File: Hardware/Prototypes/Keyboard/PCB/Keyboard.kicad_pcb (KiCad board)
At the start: 2 copper layers, 30.5 x 18.5 mm, 21 parts, among them CON1 USB-MICRO-B, U1 ATMEGA32U4-QFN44, X1 CRYSTAL-4pin

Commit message: Added the first version of the keyboard prototype module
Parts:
- removed C3: 10n, SMD-DiscreteB:0402-1005
- removed CON1: USB-MICRO-B, SMD-Connectors:USB-MICRO
- added USB1: TO HOST, Edge-Connectors:USB_EDGE, B.Cu at (149.0, 104.8)
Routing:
- net GNDD: track 14.8 -> 0.00 mm
- net Net-(R2-Pad2): track 2.57 -> 13.5 mm, vias 0 -> 1
- net Net-(R1-Pad1): track 2.71 -> 13.7 mm, vias 0 -> 1
- net +5VD: track 4.87 -> 13.0 mm, vias 0 -> 1
- net GND: track 110.6 -> 117.9 mm
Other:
- board size 30.5 x 18.5 mm -> 44.2 x 18.5 mm
- rule solder_mask_min_width: 0.1524 -> 0.0762

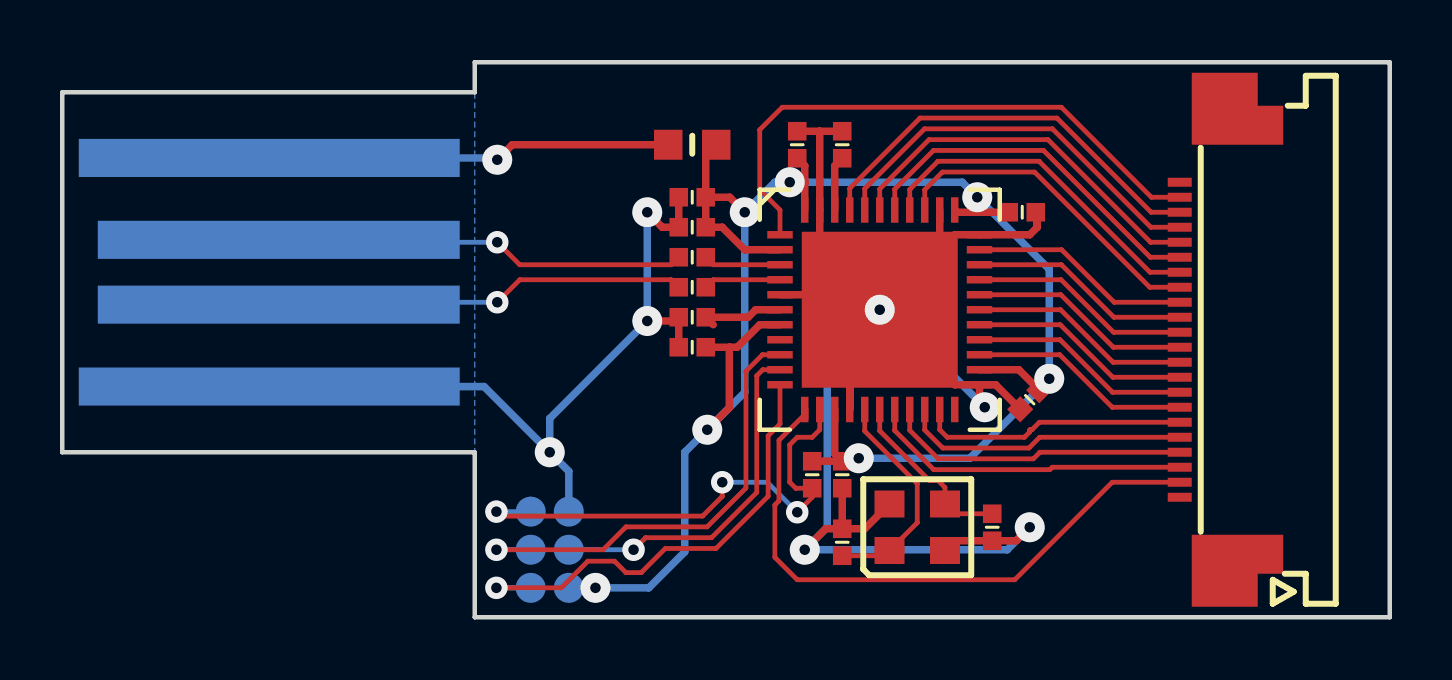
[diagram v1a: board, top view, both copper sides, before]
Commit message: More work on the keyboard
Also an attempt to make an I2C based keyboard
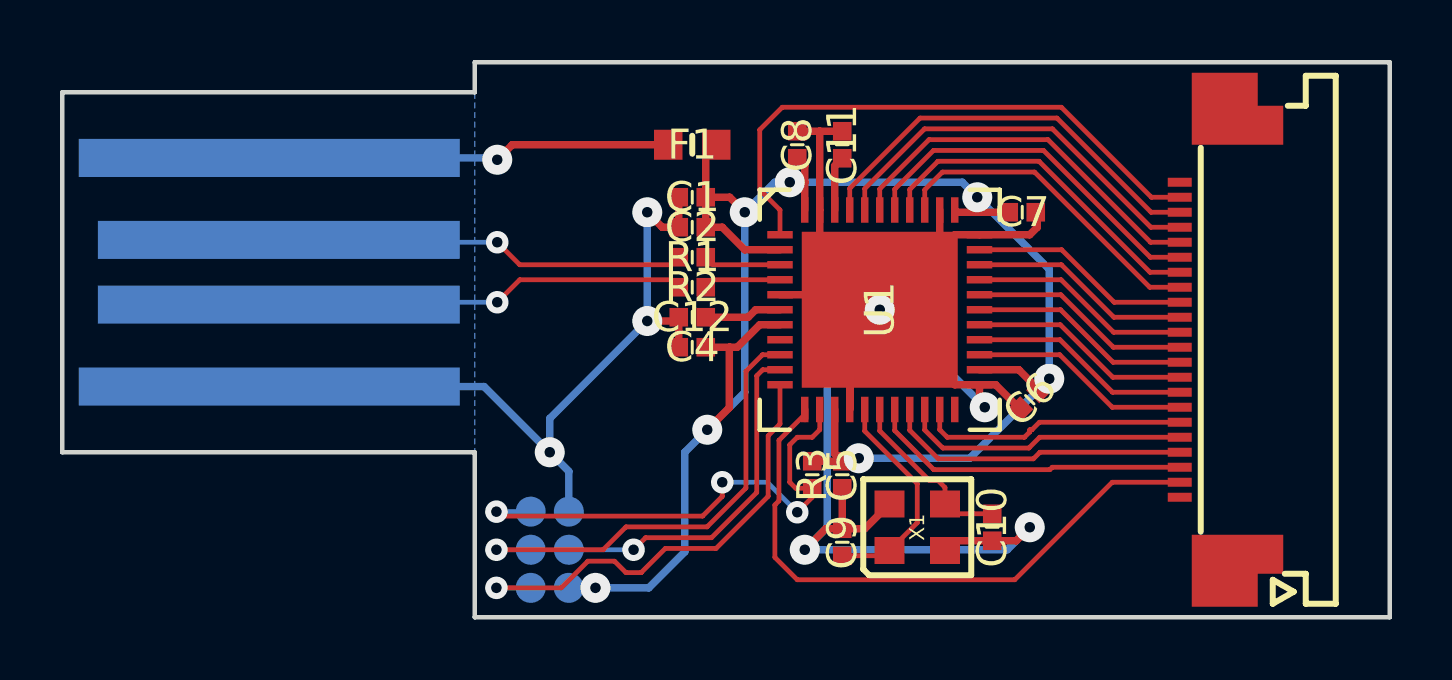
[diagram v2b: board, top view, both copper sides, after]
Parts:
- C1, C11, C12, C2, C4, C5, C6, C7, C8: footprint SMD-DiscreteB:0402-1005 -> SMD-DiscreteB:C-0402-1005
- C10, C9: value 22p -> 10p; footprint SMD-DiscreteB:0402-1005 -> SMD-DiscreteB:C-0402-1005
- R1, R2, R3: footprint SMD-DiscreteB:0402-1005 -> SMD-DiscreteB:R-0402-1005
- X1: value CRYSTAL-4pin -> ABM10-16.000MHZ-D30-T3
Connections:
- KB1 pad 19: /ROW_08 -> /ROW_07
- KB1 pad 20: /ROW_07 -> /ROW_08
- KB1 pad 4: /COL_10 -> /COL_11
- KB1 pad 5: /COL_11 -> /COL_10
- U1 pad 19: /COL_10 -> /COL_11
- U1 pad 20: /COL_11 -> /COL_10
- U1 pad 40: /ROW_08 -> /ROW_07
- U1 pad 41: /ROW_07 -> /ROW_08
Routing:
- net /COL_11: track 9.58 -> 10.2 mm
- net /COL_10: track 10.2 -> 9.58 mm
- net /ROW_08: track 13.4 -> 14.0 mm
- net /ROW_07: track 14.0 -> 13.4 mm

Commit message: Keyboard update
Version 1.1
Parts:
- removed USB1: TO HOST, Edge-Connectors:USB_EDGE
- added C3: 100n, SMD-DiscreteB:C-0402-1005, F.Cu at (160.5, 100.5)
- added D1: STATUS, SMD-DiscreteB:LED-0402-1005, F.Cu at (156.8, 110.2)
- added P1: USB_OTG, SMD-Connectors:USB-MICRO-MOLEX-47491-0001, F.Cu at (145.0, 105.1)
- added R4: 1M, SMD-DiscreteB:R-0402-1005, F.Cu at (156.8, 108.2)
- added R5: 1k, SMD-DiscreteB:R-0402-1005, F.Cu at (156.8, 111.2)
- added SW1: RESET, SMD-Switches:KSR251GLFS, F.Cu at (149.8, 113.8)
- C10: value 10p -> 15p
- C11: value 100n -> 1µ
- C12: value 1µ -> 4n7
- C8: value 100n -> 15p
- C9: value 10p -> 100n
- F1: footprint SMD-DiscreteB:0603-1608 -> SMD-DiscreteB:F-0603-1608
- ISP1: footprint SMD-Connectors:ISP-PADS_1mm27 -> SMD-Connectors:ISP-PADS_2mm54; moved to F.Cu
- moved C8 14.1 mm to (163.2, 114.2)
- moved C9 13.3 mm to (161.5, 100.5)
- moved C11 7.62 mm to (156.8, 106.2), turned to 180 degrees
- moved ISP1 7.25 mm to (159.2, 113.8), turned to 180 degrees
- moved R3 6.39 mm to (155.2, 114.8), turned to 90 degrees
- moved C12 3.00 mm to (156.8, 109.2)
- moved C10 1.80 mm to (168.2, 114.2)
- moved C7 1.60 mm to (168.8, 104.0), turned to 315 degrees
- moved X1 1.58 mm to (165.8, 113.8)
- moved KB1 1.50 mm to (171.5, 107.0)
- moved C6 0.71 mm to (168.5, 108.5), turned to 0 degrees
- moved C5 0.25 mm to (161.8, 111.2), turned to 0 degrees
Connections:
- C11 pad 1: /VARef -> /VUCap
- C12 pad 1: /VUCap -> GND
- C12 pad 2: GND -> GNDPWR
- C8 pad 1: +5V -> Net-(C8-Pad1)
- C9 pad 1: Net-(C9-Pad1) -> /VARef
- KB1 pad 1: (no net) -> /LED
- KB1 pad 22: (no net) -> /TMP
- KB1 pad 4: /COL_11 -> /COL_10
- KB1 pad 5: /COL_10 -> /COL_11
- U1 pad 12: /COL_9 -> /LED
- U1 pad 16: Net-(C9-Pad1) -> Net-(C8-Pad1)
- U1 pad 18: /COL_12 -> /COL_9
- U1 pad 19: /COL_11 -> /COL_12
- U1 pad 21: /COL_8 -> /COL_11
- U1 pad 22: (no net) -> /COL_8
- U1 pad 8: (no net) -> /TMP
- X1 pad 1: Net-(C9-Pad1) -> Net-(C8-Pad1)
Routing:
- net GND: track 117.9 -> 53.3 mm, vias 7 -> 15
- net +5V: track 63.4 -> 28.0 mm, vias 7 -> 9
- net /LED: track 0.00 -> 16.6 mm, vias 0 -> 2
- net /TMP: track 0.00 -> 15.3 mm, vias 0 -> 2
- net +5VD: track 13.0 -> 0.00 mm, vias 1 -> 0
- net /RESET: track 17.4 -> 4.65 mm, vias 3 -> 0
- net /COL_9: track 20.8 -> 9.79 mm
- net /COL_10: track 9.58 -> 0.00 mm
- net /MISO: track 15.7 -> 6.35 mm
- net /SCK: track 15.6 -> 6.52 mm
- net Net-(P1-Pad2): track 13.7 -> 5.21 mm, vias 1 -> 0
- net Net-(P1-Pad3): track 13.5 -> 5.21 mm, vias 1 -> 0
- net Net-(C8-Pad1): track 0.00 -> 7.81 mm
- net Net-(C9-Pad1): track 7.46 -> 0.00 mm
- net GNDPWR: track 0.00 -> 5.58 mm
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- added copper zone on F.Cu, net +5V
- added copper zone on Supply.Cu, net +5V
- added copper zone on F.Cu, net +5VD
- added copper zone on F.Cu, net GND
- added copper zone on Ground.Cu, net GND
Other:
- board size 44.2 x 18.5 mm -> 32 x 18 mm
- copper layers 2 -> 4
- net class Default: clearance 0.2 -> 0.127; via_dia 0.75 -> 0.4572; via_drill 0.35 -> 0.254
- net class Power: clearance 0.2 -> 0.127; via_dia 1 -> 0.4572; via_drill 0.5 -> 0.254
- rule trace_clearance: 0.2 -> 0.127
- rule trace_min: 0.1524 -> 0.127
- rule via_min_drill: 0.3302 -> 0.254
- rule via_min_size: 0.6858 -> 0.4572
- board text added: "1"
- board text added: "22"
- board text added: "USB Keyboard v1.1 RasmusB 2016 Psion Series 5/5mx"
- board text removed: "USB Keyboard RasmusB 2015 for Psion Series 5/5mx"
- board text removed: "v1.0"

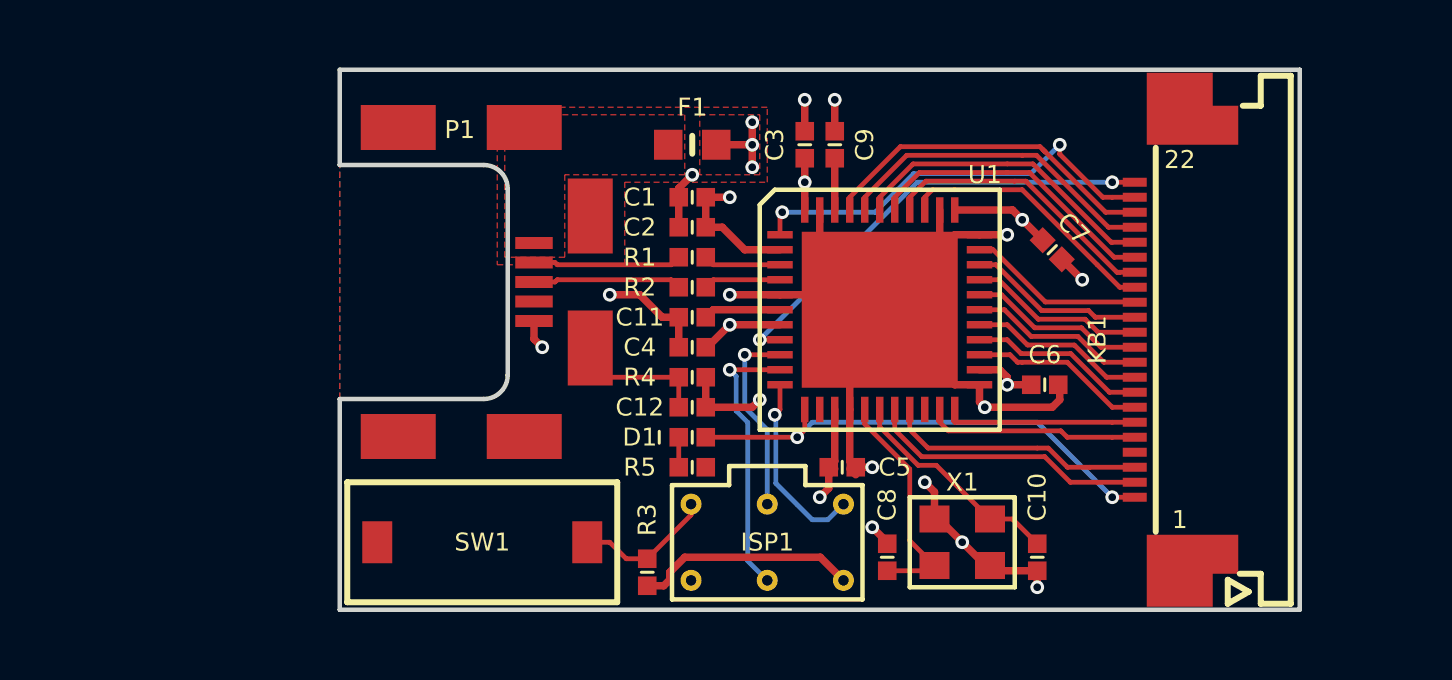
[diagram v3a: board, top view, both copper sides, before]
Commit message: Reverted to 2-layer board
Because it fits and is cheaper
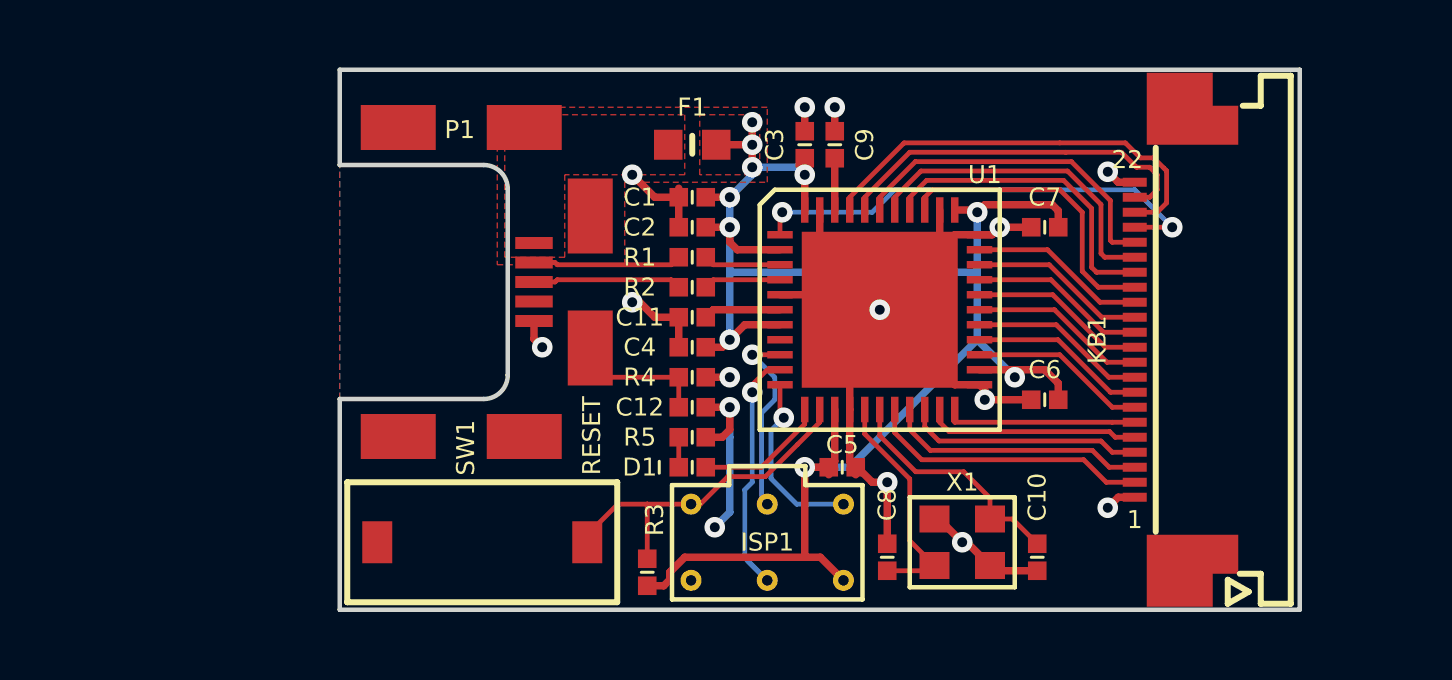
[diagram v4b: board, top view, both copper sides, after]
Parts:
- moved D1 1.00 mm to (156.8, 111.2)
- moved R5 1.00 mm to (156.8, 110.2)
- moved C7 0.79 mm to (168.5, 103.2), turned to 180 degrees
- moved C6 0.50 mm to (168.5, 109.0), turned to 180 degrees
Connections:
- KB1 pad 1: /LED -> GND
- KB1 pad 22: /TMP -> GND
- U1 pad 1: /ROW_01 -> /ROW_07
- U1 pad 40: /ROW_07 -> /ROW_01
- U1 pad 8: /TMP -> (no net)
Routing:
- net +5V: track 28.0 -> 62.2 mm, vias 9 -> 10
- net /TMP: track 15.3 -> 0.00 mm, vias 2 -> 0
- net /LED: track 16.6 -> 4.38 mm, vias 2 -> 0
- net /COL_10: track 0.00 -> 7.93 mm
- net /RESET: track 4.65 -> 11.8 mm
- net /ROW_07: track 11.0 -> 15.9 mm, vias 0 -> 2
- net GND: track 53.3 -> 56.5 mm
- net /ROW_08: track 11.6 -> 14.4 mm
- net /ROW_01: track 14.4 -> 12.5 mm, vias 2 -> 0
- net /ROW_05: track 8.87 -> 10.5 mm
- net /MOSI: track 9.21 -> 10.4 mm
- net /COL_1: track 9.41 -> 10.6 mm
- net /ROW_02: track 9.94 -> 10.9 mm
- net /ROW_06: track 10.5 -> 11.3 mm
- removed copper zone on Supply.Cu, net +5V
- removed copper zone on Ground.Cu, net GND
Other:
- copper layers 4 -> 2
- net class Default: clearance 0.127 -> 0.1524; via_dia 0.4572 -> 0.6858; via_drill 0.254 -> 0.3302
- net class Power: clearance 0.127 -> 0.1524; via_dia 0.4572 -> 0.6858; via_drill 0.254 -> 0.3302
- rule trace_clearance: 0.127 -> 0.1524
- rule via_min_drill: 0.254 -> 0.3302
- rule via_min_size: 0.4572 -> 0.6858

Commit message: Further stuff done to prepare for prototypes
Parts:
- SW1: footprint SMD-Switches:KSR251GLFS -> SMD-Switches:ALPS-SKRMAAE010
- moved SW1 1.52 mm to (151.2, 113.5), turned to 90 degrees
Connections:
- net +5VD renamed VBUS
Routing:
- net /RESET: track 11.8 -> 13.6 mm

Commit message: Major data dump
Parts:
- P1: footprint SMD-Connectors:USB-MICRO-MOLEX-47491-0001 -> SMD-Connectors:USB-MICRO-10104110-0001LF
- SW1: value RESET -> RST
- moved R3 6.67 mm to (156.8, 108.2), turned to 180 degrees
- moved R4 6.49 mm to (150.5, 110.0)
- moved C12 6.25 mm to (150.5, 109.0)
- moved P1 4.51 mm to (149.0, 103.0)
- moved D1 1.00 mm to (156.8, 110.2), turned to 180 degrees
- moved R5 1.00 mm to (156.8, 109.2)
- moved SW1 0.90 mm to (152.0, 113.0)
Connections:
- net Net-(P1-Pad2) renamed /BUS-
- net Net-(P1-Pad3) renamed /BUS+
- net Net-(R1-Pad2) renamed /D-
- net Net-(R2-Pad1) renamed /D+
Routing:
- net +5V: track 62.2 -> 55.2 mm, vias 10 -> 8
- net VBUS: track 0.00 -> 3.59 mm
- net GND: track 56.5 -> 53.1 mm, vias 15 -> 12
- net /LED: track 4.38 -> 7.35 mm
- net GNDPWR: track 5.58 -> 3.42 mm
- net /BUS-: track 5.21 -> 4.03 mm
- net /BUS+: track 5.21 -> 4.51 mm
- net /RESET: track 13.6 -> 14.2 mm
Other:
- board size 32 x 18 mm -> 28 x 18 mm
- rule pad_to_mask_clearance: 0.0762 -> 0.05
- rule solder_mask_min_width: 0.0762 -> 0.05
- board text added: "USB Keyboard v1.1 RasmusB 2017 Psion Series 5/5mx"
- board text removed: "USB Keyboard v1.1 RasmusB 2016 Psion Series 5/5mx"
